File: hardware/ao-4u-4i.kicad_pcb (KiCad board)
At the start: 4 copper layers, 100 x 85 mm, 207 parts, among them J101 TNG-Power-TOP, J102 TNG-Power-BTM, J103 TNG-Data-TOP, J104 TNG-Data-BTM, P102 Debug, P103 PE, P201 INPUT0, P202 INPUT1, P203 INPUT2, P204 INPUT3, Q101 FDS8449, SW101 BOOT, T101 744273222, U101 STM32F070CBT6, U102 AZ1117EH, U103 82400152, U104 TEL10, U105 TLP293, U106 STEF01, U201 ADS8698, U202 TLP293, U203 ISO7741DWR, U204 TPS7A6650QDGNRQ1, U205 TPS7A6633QDGNRQ1, X101 TBD

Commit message: placement draft
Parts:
- removed R230, R231, R232: 10M, kicad-libraries:R0402F
- removed R233, R235, R237, R239, R241, R243, R245, R247: 0, kicad-libraries:R0402F
- removed R234, R236, R238, R240, R242, R244, R246, R248: 1.1k, kicad-libraries:R0402F
- removed R251, R252: 4.7k, kicad-libraries:R0402F
- removed R253, R256, R257: TBD, kicad-libraries:R0402F
- added C247: 4.7uF/50V, kicad-libraries:C1206, F.Cu at (131.5, 224.0)
- added C248: 10nF/30V, kicad-libraries:C0603F, F.Cu at (145.4, 223.2)
- added C249: 10nF/30V, kicad-libraries:C0603F, F.Cu at (160.0, 206.6)
- added C250: 100nF/100V, kicad-libraries:C0805, F.Cu at (126.6, 122.8)
- added C251: 4.7uF/50V, kicad-libraries:C1206, F.Cu at (145.5, 204.3)
- added C252: 4.7uF/50V, kicad-libraries:C1206, F.Cu at (131.5, 220.8)
- added C253: 10nF/30V, kicad-libraries:C0603F, F.Cu at (163.9, 206.6)
- added C254: 10nF/30V, kicad-libraries:C0603F, F.Cu at (154.6, 216.8)
- added C255: 4.7uF/50V, kicad-libraries:C1206, F.Cu at (121.6, 120.3)
- added C256: 1uF/50V, kicad-libraries:C1206, F.Cu at (131.5, 217.6)
- added C257: 4.7uF/50V, kicad-libraries:C1206, F.Cu at (125.1, 225.2)
- added C258: 100nF/30V, kicad-libraries:C0603F, F.Cu at (168.8, 201.4)
- added C259: 4.7uF/50V, kicad-libraries:C1206, F.Cu at (119.4, 120.3)
- added C260: 4.7uF/50V, kicad-libraries:C1206, F.Cu at (153.4, 197.9)
- added C261: 4.7uF/50V, kicad-libraries:C1206, F.Cu at (118.3, 232.1)
- added C262: 4.7uF/50V, kicad-libraries:C1206, F.Cu at (121.6, 115.8)
- added C263: 4.7uF/50V, kicad-libraries:C1206, F.Cu at (125.1, 228.4)
- added C264: 4.7uF/50V, kicad-libraries:C1206, F.Cu at (123.8, 231.6)
- added C265: 4.7uF/50V, kicad-libraries:C1206, F.Cu at (112.8, 232.1)
- added C266: 4.7uF/50V, kicad-libraries:C1206, F.Cu at (128.7, 211.2)
- added D217: SMBJ18A, kicad-libraries:SMB, F.Cu at (100.2, 119.5)
- added D218: SMBJ18A, kicad-libraries:SMB, F.Cu at (100.2, 135.5)
- added D219: DESD1P0RFW, kicad-libraries:SOT23-3, F.Cu at (106.3, 117.9)
- added D220: DESD1P0RFW, kicad-libraries:SOT23-3, F.Cu at (141.4, 223.2)
- added D221: SMBJ18A, kicad-libraries:SMB, F.Cu at (100.2, 123.5)
- added D222: SMBJ18A, kicad-libraries:SMB, F.Cu at (100.2, 139.5)
- added D223: DESD1P0RFW, kicad-libraries:SOT23-3, F.Cu at (154.1, 213.6)
- added D224: DESD1P0RFW, kicad-libraries:SOT23-3, F.Cu at (137.9, 228.4)
- added L203: FB, kicad-libraries:C0603F, F.Cu at (145.8, 225.4)
- added L204: FB, kicad-libraries:C0603F, F.Cu at (149.7, 225.9)
- added L205: FB, kicad-libraries:C0603F, F.Cu at (153.6, 223.7)
- added L206: FB, kicad-libraries:C0603F, F.Cu at (158.5, 218.1)
- added L207: FB, kicad-libraries:C0603F, F.Cu at (162.0, 213.5)
- added L208: 33uH, kicad-libraries:SRN6045, F.Cu at (126.9, 118.8)
- added L209: FB, kicad-libraries:C0603F, F.Cu at (154.4, 221.3)
- added L210: FB, kicad-libraries:C0603F, F.Cu at (145.8, 230.1)
- added RP205: 470, kicad-libraries:4X0402, F.Cu at (165.9, 218.3)
- added U206: TPS560430YDBVR, kicad-libraries:SOT23-6, F.Cu at (126.7, 125.3)
- added U207: TPS7A3001DGNR, kicad-libraries:MSOP-8-EP, F.Cu at (214.4, 191.5)
- added U208: TPS7A4901DGNR, kicad-libraries:MSOP-8-EP, F.Cu at (208.6, 190.4)
- added U209: LTC3261, kicad-libraries:MSOP12_EXP, F.Cu at (219.1, 191.7)
- C201, C202, C203, C204, C207: value 27nF -> 100nF/30V; footprint kicad-libraries:C1206 -> kicad-libraries:C0603F
- C205, C206: value 27nF -> 1nF; footprint kicad-libraries:C1206 -> kicad-libraries:C0603F
- C208: value 27nF -> 4.7uF/30V
- C209, C211, C212, C213, C215: value 2700pF -> 100nF/30V
- C210, C214, C216: value 2700pF -> 4.7uF/30V; footprint kicad-libraries:C0603F -> kicad-libraries:C1206
- C217, C218, C219, C220, C221, C222, C238: value 10nF -> 100nF/30V; footprint kicad-libraries:C0402F -> kicad-libraries:C0603F
- C223, C224: value 10nF -> 1nF; footprint kicad-libraries:C0402F -> kicad-libraries:C0603F
- C225, C246: value 22uF -> 100nF/30V; footprint kicad-libraries:C1206 -> kicad-libraries:C0603F
- C226, C228, C236: value 1uF -> 4.7uF/30V; footprint kicad-libraries:C0402F -> kicad-libraries:C1206
- C227, C229, C237: value 1uF -> 100nF/30V; footprint kicad-libraries:C0402F -> kicad-libraries:C0603F
- C230: value 10µF -> 100nF/30V; footprint kicad-libraries:C1206 -> kicad-libraries:C0603F
- C231: value 10µF -> 100nF/30V; footprint kicad-libraries:C1206 -> kicad-libraries:C0603F; moved to F.Cu
- C232: value 22uF -> 4.7uF/30V
- C234: value 100µF/35V -> 100nF/30V; footprint kicad-libraries:ELKO_83 -> kicad-libraries:C0603F
- C239: value 10nF -> 2.2uF/30V; footprint kicad-libraries:C0402F -> kicad-libraries:C1206
- C240, C241, C243: value 1uF -> 4.7uF/50V; footprint kicad-libraries:C0402F -> kicad-libraries:C1206
- C242: value 1uF -> 2.2uF/30V; footprint kicad-libraries:C0402F -> kicad-libraries:C1206
- C244: value 100nF -> 4.7uF/50V; footprint kicad-libraries:C0402F -> kicad-libraries:C1206
- C245: value 100nF -> 100nF/30V; footprint kicad-libraries:C0402F -> kicad-libraries:C0603F
- D201, D202, D213, D214: value CDSOD323-T12C -> SMBJ18A; footprint kicad-libraries:SOD-323 -> kicad-libraries:SMB
- D211, D212, D215, D216: value CDSOD323-T12C -> DESD1P0RFW; footprint kicad-libraries:SOD-323 -> kicad-libraries:SOT23-3
- R201, R202, R203, R204, R205, R206: value 100 -> 15p
- R207, R208: value 100 -> 15kp
- R209: value DNP -> 10k; footprint kicad-libraries:R0805 -> kicad-libraries:R0402F
- R210: value 124 -> 10k; footprint kicad-libraries:R0805 -> kicad-libraries:R0402F
- R211, R213, R215: value DNP -> 15p; footprint kicad-libraries:R0805 -> kicad-libraries:RMELF
- R212, R214, R216: value 124 -> 15p; footprint kicad-libraries:R0805 -> kicad-libraries:RMELF
- R217, R218: value 1k -> 15kp; footprint kicad-libraries:R0603F -> kicad-libraries:RMELF
- R219, R220: value 1k -> 10k; footprint kicad-libraries:R0603F -> kicad-libraries:R0402F
- R221: value 1k -> 4.7k; footprint kicad-libraries:R0603F -> kicad-libraries:R0402F
- R222: value 1k -> 127k
- R223: value 1k -> 1.37M
- R224: value 1k -> 110k
- R225, R226: value 10M -> 9.42k; footprint kicad-libraries:R0402F -> kicad-libraries:R0603F
- R227: value 10M -> 110k; footprint kicad-libraries:R0402F -> kicad-libraries:R0603F
- R228: value 10M -> 374k; footprint kicad-libraries:R0402F -> kicad-libraries:R0603F
- R229: value 10M -> 22.1k; footprint kicad-libraries:R0402F -> kicad-libraries:R0603F
- R254, RP201, RP202, RP203, RP204: moved to F.Cu
- U201: value ADS8698 -> DAC8760; footprint kicad-libraries:TSSOP38 -> kicad-libraries:TSSOP24-44-PWR
- U202: value TLP293 -> DAC8760; footprint kicad-libraries:SOP4 -> kicad-libraries:TSSOP24-44-PWR
- U204: value TPS7A6650QDGNRQ1 -> DAC8760; footprint kicad-libraries:MSOP-8-EP -> kicad-libraries:TSSOP24-44-PWR; moved to B.Cu
- U205: value TPS7A6633QDGNRQ1 -> DAC8760; footprint kicad-libraries:MSOP-8-EP -> kicad-libraries:TSSOP24-44-PWR
- moved R217 147.1 mm to (123.6, 234.5), turned to 0 degrees
- moved R210 143.0 mm to (117.1, 234.7), turned to 0 degrees
- moved C201 142.2 mm to (150.5, 221.3), turned to 0 degrees
- moved C238 142.0 mm to (136.3, 233.8), turned to 0 degrees
- moved R201 141.9 mm to (136.8, 225.2)
- moved C202 135.8 mm to (162.4, 215.8), turned to 0 degrees
- moved C234 135.5 mm to (171.1, 208.3)
- moved C209 135.2 mm to (150.7, 216.8), turned to 0 degrees
- moved C225 131.6 mm to (149.7, 230.6), turned to 0 degrees
- moved L202 130.9 mm to (158.5, 215.8), turned to 0 degrees
- moved R209 130.2 mm to (172.1, 200.0), turned to 0 degrees
- moved R254 128.5 mm to (111.4, 234.7), turned to 0 degrees
- moved L201 128.3 mm to (167.2, 208.9), turned to 0 degrees
- moved C204 127.6 mm to (149.7, 228.2), turned to 0 degrees
- moved R203 126.5 mm to (130.4, 226.9)
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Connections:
- C201 pad 1: Net-(C201-Pad1) -> AGND
- C201 pad 2: AGND -> Net-(C201-Pad2)
- C202 pad 1: Net-(C202-Pad1) -> AGND
- C202 pad 2: AGND -> Net-(C202-Pad2)
- C203 pad 1: Net-(C203-Pad1) -> AGND
- C203 pad 2: AGND -> Net-(C203-Pad2)
- C204 pad 1: Net-(C204-Pad1) -> AGND
- C204 pad 2: AGND -> Net-(C204-Pad2)
- C205 pad 2: AGND -> Net-(C205-Pad2)
- C206 pad 2: AGND -> Net-(C206-Pad2)
- C207 pad 1: Net-(C207-Pad1) -> AGND
- C207 pad 2: AGND -> +15V
- C208 pad 1: Net-(C208-Pad1) -> AGND
- C208 pad 2: AGND -> +15V
- C209 pad 1: Net-(C209-Pad1) -> AGND
- C209 pad 2: AGND -> +15V
- C210 pad 1: Net-(C210-Pad1) -> AGND
- C210 pad 2: AGND -> +15V
- C211 pad 1: Net-(C211-Pad1) -> AGND
- C211 pad 2: AGND -> Net-(C211-Pad2)
- C212 pad 1: Net-(C212-Pad1) -> AGND
- C212 pad 2: AGND -> Net-(C212-Pad2)
- C213 pad 1: Net-(C213-Pad1) -> -15V
- C214 pad 1: Net-(C214-Pad1) -> -15V
- C215 pad 1: Net-(C215-Pad1) -> -15V
- C216 pad 1: Net-(C216-Pad1) -> -15V
- C217 pad 1: AIN6_P -> AGND
- C217 pad 2: AIN6_N -> DVDD
- C218 pad 1: AIN0_P -> AGND
- C218 pad 2: AIN0_N -> Net-(C218-Pad2)
- C219 pad 1: AIN1_P -> AGND
- C219 pad 2: AIN1_N -> Net-(C219-Pad2)
- C220 pad 1: AIN7_P -> AGND
- C220 pad 2: AIN7_N -> Net-(C220-Pad2)
- C221 pad 1: AIN4_P -> AGND
- C221 pad 2: AIN4_N -> Net-(C221-Pad2)
- C222 pad 1: AIN2_P -> AGND
- C222 pad 2: AIN2_N -> Net-(C222-Pad2)
- C223 pad 1: AIN3_P -> Net-(C223-Pad1)
- C223 pad 2: AIN3_N -> Net-(C223-Pad2)
- C224 pad 1: AIN5_P -> Net-(C224-Pad1)
- C224 pad 2: AIN5_N -> Net-(C224-Pad2)
- C225 pad 1: AVDD -> AGND
- C225 pad 2: AGND -> +15V
- C226 pad 1: DVDD -> AGND
- C226 pad 2: AGND -> +15V
- C227 pad 1: AVDD -> AGND
- C227 pad 2: AGND -> +15V
- C228 pad 2: Net-(C228-Pad2) -> +15V
- C229 pad 1: AVDD -> AGND
- C229 pad 2: AGND -> Net-(C229-Pad2)
- C230 pad 1: DVDD -> AGND
- C230 pad 2: AGND -> Net-(C230-Pad2)
- C231 pad 1: AGND -> -15V
- C231 pad 2: Net-(C231-Pad2) -> AGND
- C232 pad 1: AGND -> -15V
- C232 pad 2: Net-(C228-Pad2) -> AGND
- C234 pad 1: VCC -> -15V
- C236 pad 1: AGND -> -15V
- C236 pad 2: Net-(C236-Pad2) -> AGND
- C239 pad 2: Net-(C239-Pad2) -> VCC
- C240 pad 1: AVDD -> AGND
- C240 pad 2: AGND -> +15V
- C241 pad 1: DVDD -> AGND
- C241 pad 2: AGND -> Net-(C241-Pad2)
- C242 pad 1: AVDD -> AGND
- C242 pad 2: AGND -> VCC
- C243 pad 1: DVDD -> AGND
- C243 pad 2: AGND -> Net-(C241-Pad2)
- C244 pad 2: AVDD -> Net-(C244-Pad2)
- C245 pad 2: DVDD -> VCC
- C246 pad 1: DVDD -> Net-(C241-Pad2)
- D201 pad 1: Net-(C201-Pad1) -> Net-(C201-Pad2)
- D202 pad 1: Net-(C202-Pad1) -> Net-(C202-Pad2)
- D211 pad 1: Net-(C203-Pad1) -> -15V
- D211 pad 2: AGND -> +15V
- D212 pad 1: Net-(C204-Pad1) -> -15V
- D212 pad 2: AGND -> +15V
- D213 pad 1: Net-(C205-Pad1) -> Net-(C203-Pad2)
- D214 pad 1: Net-(C206-Pad1) -> Net-(C204-Pad2)
- D215 pad 1: Net-(C207-Pad1) -> -15V
- D215 pad 2: AGND -> +15V
- D216 pad 1: Net-(C208-Pad1) -> -15V
- D216 pad 2: AGND -> +15V
- L201 pad 1: Net-(C236-Pad2) -> Net-(L201-Pad1)
- L201 pad 2: VCC -> Net-(C201-Pad2)
- L202 pad 1: Net-(C237-Pad2) -> Net-(C258-Pad1)
- L202 pad 2: VCC -> Net-(C255-Pad2)
- P201 pad 2: Net-(P201-Pad2) -> Net-(C201-Pad2)
- P201 pad 3: Net-(P201-Pad3) -> Net-(C203-Pad2)
- P202 pad 2: Net-(P202-Pad2) -> Net-(C202-Pad2)
- P202 pad 3: Net-(P202-Pad3) -> Net-(C204-Pad2)
- P203 pad 2: Net-(P203-Pad2) -> Net-(C219-Pad2)
- P203 pad 3: Net-(P203-Pad3) -> Net-(C221-Pad2)
- P204 pad 2: Net-(P204-Pad2) -> Net-(C220-Pad2)
- P204 pad 3: Net-(P204-Pad3) -> Net-(C222-Pad2)
- R201 pad 1: Net-(P201-Pad2) -> Net-(L201-Pad1)
- R201 pad 2: Net-(C201-Pad1) -> Net-(R201-Pad2)
- R202 pad 1: Net-(P201-Pad3) -> Net-(L201-Pad1)
- R202 pad 2: Net-(C202-Pad1) -> Net-(C205-Pad2)
- R203 pad 1: Net-(P202-Pad2) -> Net-(C203-Pad2)
- R203 pad 2: Net-(C203-Pad1) -> Net-(D215-Pad3)
- R204 pad 1: Net-(P202-Pad3) -> Net-(L203-Pad1)
- R204 pad 2: Net-(C204-Pad1) -> Net-(R204-Pad2)
- R205 pad 1: Net-(P203-Pad2) -> Net-(L203-Pad1)
- R205 pad 2: Net-(C205-Pad1) -> Net-(C206-Pad2)
- R206 pad 1: Net-(P203-Pad3) -> Net-(C204-Pad2)
- R206 pad 2: Net-(C206-Pad1) -> Net-(D216-Pad3)
- R207 pad 1: Net-(P204-Pad2) -> Net-(R207-Pad1)
- R207 pad 2: Net-(C207-Pad1) -> AGND
- R208 pad 1: Net-(P204-Pad3) -> Net-(R208-Pad1)
- R208 pad 2: Net-(C208-Pad1) -> AGND
- R209 pad 1: AGND -> Net-(R209-Pad1)
- R209 pad 2: Net-(C201-Pad1) -> DVDD
- R210 pad 1: AGND -> Net-(R210-Pad1)
- R210 pad 2: Net-(C202-Pad1) -> Net-(C218-Pad2)
- R211 pad 1: AGND -> Net-(L204-Pad1)
- R211 pad 2: Net-(C203-Pad1) -> Net-(R211-Pad2)
- R212 pad 1: AGND -> Net-(L204-Pad1)
- R212 pad 2: Net-(C204-Pad1) -> Net-(C223-Pad2)
- R213 pad 1: AGND -> Net-(C221-Pad2)
- R213 pad 2: Net-(C205-Pad1) -> Net-(D223-Pad3)
- R214 pad 1: AGND -> Net-(L205-Pad1)
- R214 pad 2: Net-(C206-Pad1) -> Net-(R214-Pad2)
- R215 pad 1: AGND -> Net-(L205-Pad1)
- R215 pad 2: Net-(C207-Pad1) -> Net-(C224-Pad2)
- R216 pad 1: AGND -> Net-(C222-Pad2)
- R216 pad 2: Net-(C208-Pad1) -> Net-(D224-Pad3)
- R217 pad 1: Net-(C209-Pad1) -> Net-(R217-Pad1)
- R217 pad 2: Net-(C201-Pad1) -> AGND
- R218 pad 1: Net-(C210-Pad1) -> Net-(R218-Pad1)
- R218 pad 2: Net-(C202-Pad1) -> AGND
- R219 pad 1: Net-(C211-Pad1) -> Net-(R219-Pad1)
- R219 pad 2: Net-(C203-Pad1) -> Net-(C237-Pad2)
- R220 pad 1: Net-(C212-Pad1) -> Net-(R220-Pad1)
- R220 pad 2: Net-(C204-Pad1) -> Net-(C238-Pad2)
- R221 pad 1: Net-(C213-Pad1) -> Net-(R221-Pad1)
- R221 pad 2: Net-(C205-Pad1) -> DVDD
- R222 pad 1: Net-(C214-Pad1) -> Net-(R222-Pad1)
- R222 pad 2: Net-(C206-Pad1) -> AGND
- R223 pad 1: Net-(C215-Pad1) -> Net-(R222-Pad1)
- R223 pad 2: Net-(C207-Pad1) -> VCC
- R224 pad 1: Net-(C216-Pad1) -> Net-(C249-Pad2)
- R224 pad 2: Net-(C208-Pad1) -> Net-(C244-Pad2)
- R225 pad 2: Net-(C209-Pad1) -> Net-(C249-Pad2)
- R226 pad 2: Net-(C210-Pad1) -> Net-(C253-Pad2)
- R227 pad 1: AGND -> Net-(C253-Pad2)
- R227 pad 2: Net-(C211-Pad1) -> Net-(C253-Pad1)
- R228 pad 1: AGND -> Net-(R228-Pad1)
- R228 pad 2: Net-(C212-Pad1) -> Net-(C255-Pad2)
- R229 pad 2: Net-(C213-Pad1) -> Net-(R228-Pad1)
- RP206 pad 1: SPI-MOSI -> SPI-LATCH
- RP206 pad 2: SPI-CS -> SPI-MOSI
- U101 pad 11: ADC-RESET -> (no net)
- U101 pad 38: SPI-CS -> SPI-LATCH
- U201 pad 1: Net-(U201-Pad1) -> -15V
- U201 pad 10: AGND -> Net-(U201-Pad10)
- U201 pad 12: AIN6_P -> AGND
- U201 pad 13: AIN6_N -> Net-(R207-Pad1)
- U201 pad 14: AIN7_P -> Net-(C211-Pad2)
- U201 pad 15: AIN7_N -> Net-(C211-Pad2)
- U201 pad 16: AIN0_P -> (no net)
- U201 pad 17: AIN0_N -> Net-(C205-Pad1)
- U201 pad 18: AIN1_P -> (no net)
- U201 pad 19: AIN1_N -> Net-(D215-Pad3)
- U201 pad 2: _RESET -> DVDD
- U201 pad 20: AIN2_N -> (no net)
- U201 pad 21: AIN2_P -> Net-(C205-Pad2)
- U201 pad 22: AIN3_N -> Net-(R201-Pad2)
- U201 pad 23: AIN3_P -> AGND
- U201 pad 24: AIN4_N -> +15V
- U201 pad 3: AGND -> Net-(R209-Pad1)
- U201 pad 5: Net-(C231-Pad2) -> AGND
- U201 pad 7: Net-(C228-Pad2) -> _SPI-LATCH
- U201 pad 8: AGND -> _SPI-CLK
- U201 pad 9: AVDD -> _SPI-MOSI
- U202 pad 1: 3V3 -> -15V
- U202 pad 2: Net-(R253-Pad2) -> Net-(C218-Pad2)
- U202 pad 3: AGND -> Net-(R210-Pad1)
- U202 pad 4: _RESET -> AGND
- U203 pad 10: Net-(R252-Pad1) -> Net-(R221-Pad1)
- U203 pad 11: Net-(U201-Pad36) -> Net-(RP205-Pad4)
- U203 pad 12: Net-(U201-Pad37) -> Net-(RP205-Pad3)
- U203 pad 13: Net-(U201-Pad38) -> Net-(RP205-Pad2)
- U203 pad 14: Net-(U201-Pad1) -> Net-(RP205-Pad1)
- U204 pad 1: Net-(C236-Pad2) -> -15V
- U204 pad 2: Net-(C236-Pad2) -> Net-(C237-Pad2)
- U204 pad 3: (no net) -> Net-(R219-Pad1)
- U204 pad 4: Net-(C238-Pad2) -> AGND
- U204 pad 6: Net-(R256-Pad2) -> AGND
- U204 pad 7: (no net) -> _SPI-LATCH
- U204 pad 8: AVDD -> _SPI-CLK
- U204 pad EP: AGND -> -15V
- U205 pad 1: Net-(C237-Pad2) -> -15V
- U205 pad 2: Net-(C237-Pad2) -> Net-(C238-Pad2)
- U205 pad 3: (no net) -> Net-(R220-Pad1)
- U205 pad 4: Net-(C239-Pad2) -> AGND
- U205 pad 6: Net-(R257-Pad2) -> AGND
- U205 pad 7: (no net) -> _SPI-LATCH
- U205 pad 8: DVDD -> _SPI-CLK
- U205 pad EP: AGND -> -15V
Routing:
- net AGND: track 252.6 -> 33.0 mm, vias 160 -> 12
- net LED7: track 54.6 -> 0.00 mm, vias 1 -> 0
- net LED6: track 53.3 -> 0.00 mm, vias 1 -> 0
- net LED5: track 50.0 -> 0.00 mm, vias 1 -> 0
- net LED4: track 48.8 -> 0.00 mm, vias 1 -> 0
- net SPI-CS: track 48.8 -> 0.00 mm, vias 2 -> 0
- net SPI-MOSI: track 48.4 -> 0.00 mm, vias 2 -> 0
- net SPI-CLK: track 47.8 -> 0.00 mm, vias 2 -> 0
- net Net-(D210-Pad1): track 46.9 -> 0.00 mm
- net SPI-MISO: track 46.9 -> 0.00 mm, vias 2 -> 0
- net Net-(D209-Pad2): track 46.2 -> 0.00 mm
- net Net-(D210-Pad2): track 46.2 -> 0.00 mm
- net Net-(D209-Pad1): track 45.6 -> 0.00 mm
- net DVDD: track 45.2 -> 0.00 mm, vias 8 -> 0
- net Net-(D206-Pad1): track 41.0 -> 0.00 mm
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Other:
- board text added: "AO 4U 4I REV 1.0"
- board text removed: "AI 4U 4I REV 1.0"

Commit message: placement complete
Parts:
- added C267: 4.7uF/50V, kicad-libraries:C1206, F.Cu at (130.1, 107.9)
- C205, C206, C207, C208, C209, C210, C211, C212, C213, C214, C215, C216, C217, C218, C223, C224, C225, C226, C227, C228, C229, C230, C231, C232, C234, C236, C237, C238, C253, R222, R223, R226, R227, RP201, RP202, RP203, RP204, U201, U202, U205: moved to B.Cu
- D101: moved to F.Cu
- R201, R202, R204, R205, R211, R212, R214, R215: value 15p -> 15; footprint kicad-libraries:RMELF -> kicad-libraries:R0603F
- R203, R206, R213, R216: value 15p -> 15 1/2W 1%; footprint kicad-libraries:RMELF -> kicad-libraries:R1210
- R207, R208, R217, R218: value 15kp -> 15k 0.1%; footprint kicad-libraries:RMELF -> kicad-libraries:R0603F; moved to B.Cu
- moved R254 156.5 mm to (144.3, 81.7), turned to 180 degrees
- moved R221 153.8 mm to (130.3, 81.7), turned to 180 degrees
- moved C265 151.6 mm to (121.5, 80.8)
- moved C207 150.9 mm to (108.8, 84.7), turned to 180 degrees
- moved C205 147.9 mm to (106.0, 90.0), turned to 90 degrees
- moved C201 146.2 mm to (101.2, 83.8), turned to 270 degrees
- moved C213 144.5 mm to (113.2, 84.7), turned to 180 degrees
- moved C208 144.2 mm to (108.8, 83.0), turned to 180 degrees
- moved C217 144.0 mm to (115.7, 87.0), turned to 90 degrees
- moved L209 143.3 mm to (124.4, 81.2), turned to 90 degrees
- moved R201 142.6 mm to (105.0, 86.2)
- moved U207 141.4 mm to (119.2, 87.0), turned to 180 degrees
- moved C257 140.3 mm to (121.8, 84.9), turned to 90 degrees
- moved L201 139.7 mm to (103.5, 84.5), turned to 180 degrees
- moved RP205 138.3 mm to (129.6, 84.8), turned to 90 degrees
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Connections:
- L208 pad 1: Net-(C250-Pad2) -> Net-(C250-Pad1)
- U206 pad 1: Net-(C250-Pad1) -> Net-(C250-Pad2)
- U206 pad 6: Net-(C250-Pad2) -> Net-(C250-Pad1)
- U209 pad 1: AGND -> (no net)
- U209 pad 12: AGND -> (no net)
- U209 pad 3: AGND -> (no net)
- U209 pad 6: AGND -> Net-(C256-Pad1)
- U209 pad 7: AGND -> Net-(C256-Pad2)
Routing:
- net AGND: track 33.0 -> 114.3 mm, vias 12 -> 100
- net Net-(C255-Pad2): track 0.00 -> 37.2 mm, vias 0 -> 2
- net VCC: track 31.1 -> 62.6 mm
- net -15V: track 0.00 -> 29.7 mm, vias 0 -> 27
- net Net-(C241-Pad2): track 0.00 -> 14.7 mm, vias 0 -> 2
- net Net-(C258-Pad1): track 0.00 -> 14.5 mm, vias 0 -> 2
- net Net-(C221-Pad2): track 0.00 -> 13.5 mm
- net Net-(C250-Pad1): track 0.00 -> 13.0 mm
- net +15V: track 0.00 -> 11.8 mm, vias 0 -> 6
- net Net-(C244-Pad2): track 0.00 -> 11.5 mm
- net Net-(C219-Pad2): track 0.00 -> 9.62 mm
- net Net-(D223-Pad3): track 0.00 -> 9.09 mm, vias 0 -> 1
- net Net-(C263-Pad2): track 0.00 -> 7.78 mm
- net Net-(C253-Pad1): track 0.00 -> 7.10 mm
- net Net-(C251-Pad2): track 0.00 -> 5.58 mm
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
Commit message: some routing
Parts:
- moved D101 16.5 mm to (123.8, 157.3)
- moved RP204 14.8 mm to (141.1, 88.2)
- moved RP203 14.0 mm to (141.1, 86.0)
- moved RP202 13.3 mm to (141.1, 83.8)
- moved RP201 12.5 mm to (141.1, 81.5)
- moved R214 1.60 mm to (105.0, 134.2)
- moved R215 1.60 mm to (105.0, 135.8)
- moved R210 0.95 mm to (115.7, 102.9)
- moved R209 0.90 mm to (115.7, 86.9)
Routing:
- net AGND: track 114.3 -> 289.8 mm, vias 100 -> 258
- net _SPI-CLK: track 0.00 -> 81.9 mm, vias 0 -> 5
- net _SPI-LATCH: track 0.00 -> 79.6 mm, vias 0 -> 5
- net -15V: track 29.7 -> 101.9 mm, vias 27 -> 99
- net _SPI-MISO: track 0.00 -> 71.7 mm, vias 0 -> 1
- net _SPI-MOSI: track 0.00 -> 22.9 mm, vias 0 -> 1
- net SPI-LATCH: track 0.00 -> 21.8 mm, vias 0 -> 2
- net Net-(U202-Pad10): track 0.00 -> 21.1 mm
- net Net-(U204-Pad10): track 0.00 -> 20.6 mm
- net SPI-CLK: track 0.00 -> 20.5 mm, vias 0 -> 2
- net Net-(U201-Pad10): track 0.00 -> 20.4 mm
- net SPI-MOSI: track 0.00 -> 20.2 mm, vias 0 -> 2
- net SPI-MISO: track 0.00 -> 19.2 mm, vias 0 -> 2
- net +15V: track 11.8 -> 29.1 mm, vias 6 -> 15
- net Net-(C222-Pad2): track 2.40 -> 13.3 mm
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
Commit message: more routing
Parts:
- moved D101 16.8 mm to (117.8, 141.7)
- moved D224 4.83 mm to (107.2, 138.9), turned to 90 degrees
- moved D215 4.83 mm to (107.2, 91.0), turned to 90 degrees
- moved D216 4.83 mm to (107.2, 107.0), turned to 90 degrees
- moved D223 4.83 mm to (107.2, 123.0), turned to 90 degrees
- moved Fiducial_Mark 2.50 mm to (101.8, 144.0)
- moved R218 1.31 mm to (109.0, 142.2), turned to 0 degrees
- moved R207 1.27 mm to (109.0, 94.2), turned to 0 degrees
- moved R208 1.27 mm to (109.0, 110.2), turned to 0 degrees
- moved R217 1.27 mm to (109.0, 126.2), turned to 0 degrees
- moved R213 0.30 mm to (105.5, 127.0)
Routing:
- net -15V: track 101.9 -> 304.5 mm
- net +15V: track 29.1 -> 231.2 mm
- net VCC: track 62.6 -> 164.4 mm
- net Net-(D210-Pad1): track 0.00 -> 86.3 mm
- net Net-(D210-Pad2): track 0.00 -> 85.4 mm
- net Net-(D206-Pad1): track 0.00 -> 83.4 mm
- net Net-(D209-Pad1): track 0.00 -> 81.1 mm
- net Net-(D209-Pad2): track 0.00 -> 80.4 mm
- net Net-(D208-Pad1): track 0.00 -> 68.1 mm
- net Net-(D208-Pad2): track 0.00 -> 67.1 mm
- net Net-(D207-Pad1): track 0.00 -> 62.2 mm
- net Net-(D207-Pad2): track 0.00 -> 61.2 mm
- net 3V3: track 27.6 -> 56.2 mm, vias 11 -> 18
- net DVDD: track 9.08 -> 32.7 mm
- net LED7: track 0.00 -> 23.1 mm, vias 0 -> 1
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
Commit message: more routing
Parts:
- moved Fiducial_Mark 17.2 mm to (107.1, 58.0)
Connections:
- J101 pad 21: (no net) -> Net-(J101-Pad21)
- J101 pad 22: (no net) -> Net-(J101-Pad22)
- J101 pad 23: (no net) -> Net-(J101-Pad23)
- J101 pad 24: (no net) -> Net-(J101-Pad24)
- J101 pad 25: (no net) -> Net-(J101-Pad25)
- J101 pad 26: (no net) -> Net-(J101-Pad26)
- J101 pad 27: (no net) -> Net-(J101-Pad27)
- J101 pad 28: (no net) -> Net-(J101-Pad28)
- J101 pad 29: (no net) -> Net-(J101-Pad29)
- J101 pad 30: (no net) -> Net-(J101-Pad30)
- J102 pad 21: (no net) -> Net-(J102-Pad21)
- J102 pad 22: (no net) -> Net-(J102-Pad22)
- J102 pad 23: (no net) -> Net-(J102-Pad23)
- J102 pad 24: (no net) -> Net-(J102-Pad24)
- J102 pad 25: (no net) -> Net-(J102-Pad25)
- J102 pad 26: (no net) -> Net-(J102-Pad26)
- J102 pad 27: (no net) -> Net-(J102-Pad27)
- J102 pad 28: (no net) -> Net-(J102-Pad28)
- J102 pad 29: (no net) -> Net-(J102-Pad29)
- J102 pad 30: (no net) -> Net-(J102-Pad30)
- J103 pad 35: (no net) -> Net-(J103-Pad35)
- J103 pad 37: (no net) -> Net-(J103-Pad37)
- RP201 pad 1: LED0 -> 3V3
- RP201 pad 2: 3V3 -> LED0
- RP201 pad 5: Net-(D204-Pad1) -> Net-(D203-Pad1)
- RP201 pad 6: Net-(D204-Pad2) -> Net-(D203-Pad2)
- RP201 pad 7: Net-(D203-Pad1) -> Net-(D204-Pad2)
- RP201 pad 8: Net-(D203-Pad2) -> Net-(D204-Pad1)
- U101 pad 11: (no net) -> ADC-RESET
- U101 pad 2: (no net) -> Net-(U101-Pad2)
- U101 pad 20: (no net) -> Net-(U101-Pad20)
- U101 pad 21: (no net) -> Net-(U101-Pad21)
- U101 pad 22: (no net) -> Net-(U101-Pad22)
- U101 pad 26: (no net) -> Net-(U101-Pad26)
- U101 pad 27: (no net) -> Net-(U101-Pad27)
- U101 pad 28: (no net) -> Net-(U101-Pad28)
- U101 pad 3: (no net) -> Net-(U101-Pad3)
- U101 pad 34: (no net) -> Net-(U101-Pad34)
- U101 pad 37: (no net) -> Net-(U101-Pad37)
- U101 pad 4: (no net) -> Net-(U101-Pad4)
- U101 pad 42: (no net) -> Net-(U101-Pad42)
- U101 pad 43: (no net) -> Net-(U101-Pad43)
- U101 pad 46: (no net) -> Net-(U101-Pad46)
- U101 pad 7: (no net) -> Net-(U101-Pad7)
- U104 pad 7: (no net) -> Net-(U104-Pad7)
- U104 pad 8: (no net) -> Net-(U104-Pad8)
- U106 pad 12: (no net) -> Net-(U106-Pad12)
- U106 pad 2: (no net) -> Net-(U106-Pad2)
- U201 pad 16: (no net) -> Net-(U201-Pad16)
- U201 pad 18: (no net) -> Net-(U201-Pad18)
- U201 pad 20: (no net) -> Net-(U201-Pad20)
- U202 pad 16: (no net) -> Net-(U202-Pad16)
- U202 pad 18: (no net) -> Net-(U202-Pad18)
- U202 pad 20: (no net) -> Net-(U202-Pad20)
- U204 pad 16: (no net) -> Net-(U204-Pad16)
- U204 pad 18: (no net) -> Net-(U204-Pad18)
- U204 pad 20: (no net) -> Net-(U204-Pad20)
- U205 pad 16: (no net) -> Net-(U205-Pad16)
- U205 pad 18: (no net) -> Net-(U205-Pad18)
- U205 pad 20: (no net) -> Net-(U205-Pad20)
- U207 pad 7: (no net) -> Net-(U207-Pad7)
- U208 pad 3: (no net) -> Net-(U208-Pad3)
- U208 pad 7: (no net) -> Net-(U208-Pad7)
- U209 pad 1: (no net) -> Net-(U209-Pad1)
- U209 pad 12: (no net) -> Net-(U209-Pad12)
- U209 pad 3: (no net) -> Net-(U209-Pad3)
- U209 pad 6: Net-(C256-Pad1) -> Net-(U209-Pad6)
- U209 pad 7: Net-(C256-Pad2) -> Net-(U209-Pad7)
- U209 pad EXP: AGND -> Net-(U209-PadEXP)
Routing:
- net Net-(D206-Pad2): track 0.00 -> 68.7 mm
- net Net-(D204-Pad1): track 0.00 -> 67.5 mm
- net Net-(D205-Pad1): track 0.00 -> 64.5 mm
- net Net-(D205-Pad2): track 0.00 -> 64.3 mm
- net Net-(D204-Pad2): track 0.00 -> 62.6 mm
- net Net-(D203-Pad2): track 0.00 -> 52.0 mm
- net Net-(D203-Pad1): track 0.00 -> 51.1 mm
- net Net-(D206-Pad1): track 83.4 -> 68.7 mm
- net Net-(C206-Pad1): track 0.00 -> 2.09 mm
- net -15V: track 304.5 -> 302.5 mm
- net GND: track 124.6 -> 126.4 mm
- net 3V3: track 56.2 -> 55.3 mm

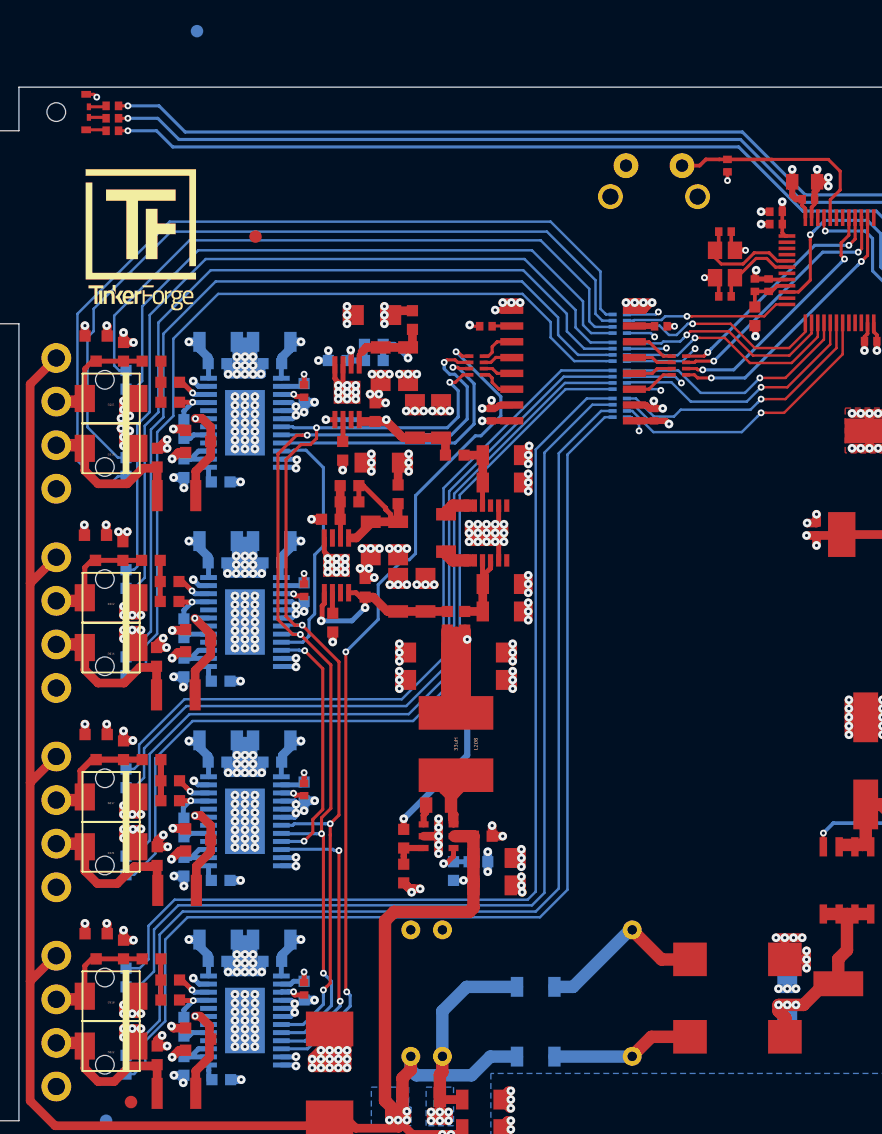
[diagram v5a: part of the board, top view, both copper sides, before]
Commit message: fix footprint spacing, fix description
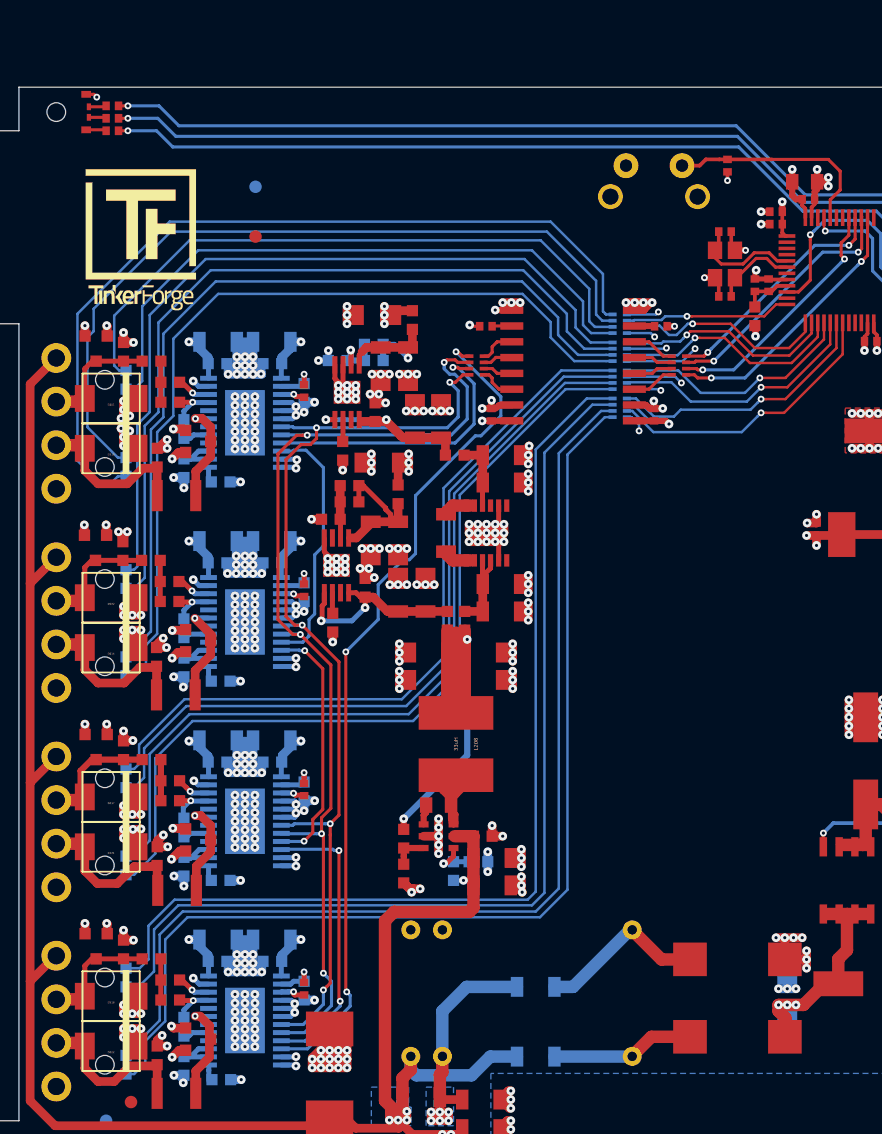
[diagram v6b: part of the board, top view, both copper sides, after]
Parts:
- moved Fiducial_Mark 13.4 mm to (111.8, 70.5)
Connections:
- J101 pad 21: Net-(J101-Pad21) -> (no net)
- J101 pad 22: Net-(J101-Pad22) -> (no net)
- J101 pad 23: Net-(J101-Pad23) -> (no net)
- J101 pad 24: Net-(J101-Pad24) -> (no net)
- J101 pad 25: Net-(J101-Pad25) -> (no net)
- J101 pad 26: Net-(J101-Pad26) -> (no net)
- J101 pad 27: Net-(J101-Pad27) -> (no net)
- J101 pad 28: Net-(J101-Pad28) -> (no net)
- J101 pad 29: Net-(J101-Pad29) -> (no net)
- J101 pad 30: Net-(J101-Pad30) -> (no net)
- J102 pad 21: Net-(J102-Pad21) -> (no net)
- J102 pad 22: Net-(J102-Pad22) -> (no net)
- J102 pad 23: Net-(J102-Pad23) -> (no net)
- J102 pad 24: Net-(J102-Pad24) -> (no net)
- J102 pad 25: Net-(J102-Pad25) -> (no net)
- J102 pad 26: Net-(J102-Pad26) -> (no net)
- J102 pad 27: Net-(J102-Pad27) -> (no net)
- J102 pad 28: Net-(J102-Pad28) -> (no net)
- J102 pad 29: Net-(J102-Pad29) -> (no net)
- J102 pad 30: Net-(J102-Pad30) -> (no net)
- J103 pad 35: Net-(J103-Pad35) -> (no net)
- J103 pad 37: Net-(J103-Pad37) -> (no net)
- U101 pad 11: ADC-RESET -> (no net)
- U101 pad 2: Net-(U101-Pad2) -> (no net)
- U101 pad 20: Net-(U101-Pad20) -> (no net)
- U101 pad 21: Net-(U101-Pad21) -> (no net)
- U101 pad 22: Net-(U101-Pad22) -> (no net)
- U101 pad 26: Net-(U101-Pad26) -> (no net)
- U101 pad 27: Net-(U101-Pad27) -> (no net)
- U101 pad 28: Net-(U101-Pad28) -> (no net)
- U101 pad 3: Net-(U101-Pad3) -> (no net)
- U101 pad 34: Net-(U101-Pad34) -> (no net)
- U101 pad 37: Net-(U101-Pad37) -> (no net)
- U101 pad 4: Net-(U101-Pad4) -> (no net)
- U101 pad 42: Net-(U101-Pad42) -> (no net)
- U101 pad 43: Net-(U101-Pad43) -> (no net)
- U101 pad 46: Net-(U101-Pad46) -> (no net)
- U101 pad 7: Net-(U101-Pad7) -> (no net)
- U104 pad 7: Net-(U104-Pad7) -> (no net)
- U104 pad 8: Net-(U104-Pad8) -> (no net)
- U106 pad 12: Net-(U106-Pad12) -> (no net)
- U106 pad 2: Net-(U106-Pad2) -> (no net)
- U201 pad 16: Net-(U201-Pad16) -> (no net)
- U201 pad 18: Net-(U201-Pad18) -> (no net)
- U201 pad 20: Net-(U201-Pad20) -> (no net)
- U202 pad 16: Net-(U202-Pad16) -> (no net)
- U202 pad 18: Net-(U202-Pad18) -> (no net)
- U202 pad 20: Net-(U202-Pad20) -> (no net)
- U204 pad 16: Net-(U204-Pad16) -> (no net)
- U204 pad 18: Net-(U204-Pad18) -> (no net)
- U204 pad 20: Net-(U204-Pad20) -> (no net)
- U205 pad 16: Net-(U205-Pad16) -> (no net)
- U205 pad 18: Net-(U205-Pad18) -> (no net)
- U205 pad 20: Net-(U205-Pad20) -> (no net)
- U207 pad 7: Net-(U207-Pad7) -> (no net)
- U208 pad 3: Net-(U208-Pad3) -> (no net)
- U208 pad 7: Net-(U208-Pad7) -> (no net)
- U209 pad 1: Net-(U209-Pad1) -> (no net)
- U209 pad 12: Net-(U209-Pad12) -> (no net)
- U209 pad 3: Net-(U209-Pad3) -> (no net)
- U209 pad 6: Net-(U209-Pad6) -> Net-(C256-Pad1)
- U209 pad 7: Net-(U209-Pad7) -> Net-(C256-Pad2)
- U209 pad EXP: Net-(U209-PadEXP) -> AGND
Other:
- board text added: "AO0"
- board text added: "AO1"
- board text added: "AO2"
- board text added: "AO3"
- board text added: "AO4"
- board text added: "AO5"
- board text added: "AO6"
- board text added: "AO7"
- board text removed: "AI0"
- board text removed: "AI1"
- board text removed: "AI2"
- board text removed: "AI3"
- board text removed: "AI4"
- board text removed: "AI5"
- board text removed: "AI6"
- board text removed: "AI7"
